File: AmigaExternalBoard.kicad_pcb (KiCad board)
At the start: 2 copper layers, 66.6 x 85.1 mm, 11 parts, among them J1 Conn_01x24, J2 Conn_01x24, J3 Conn_01x24

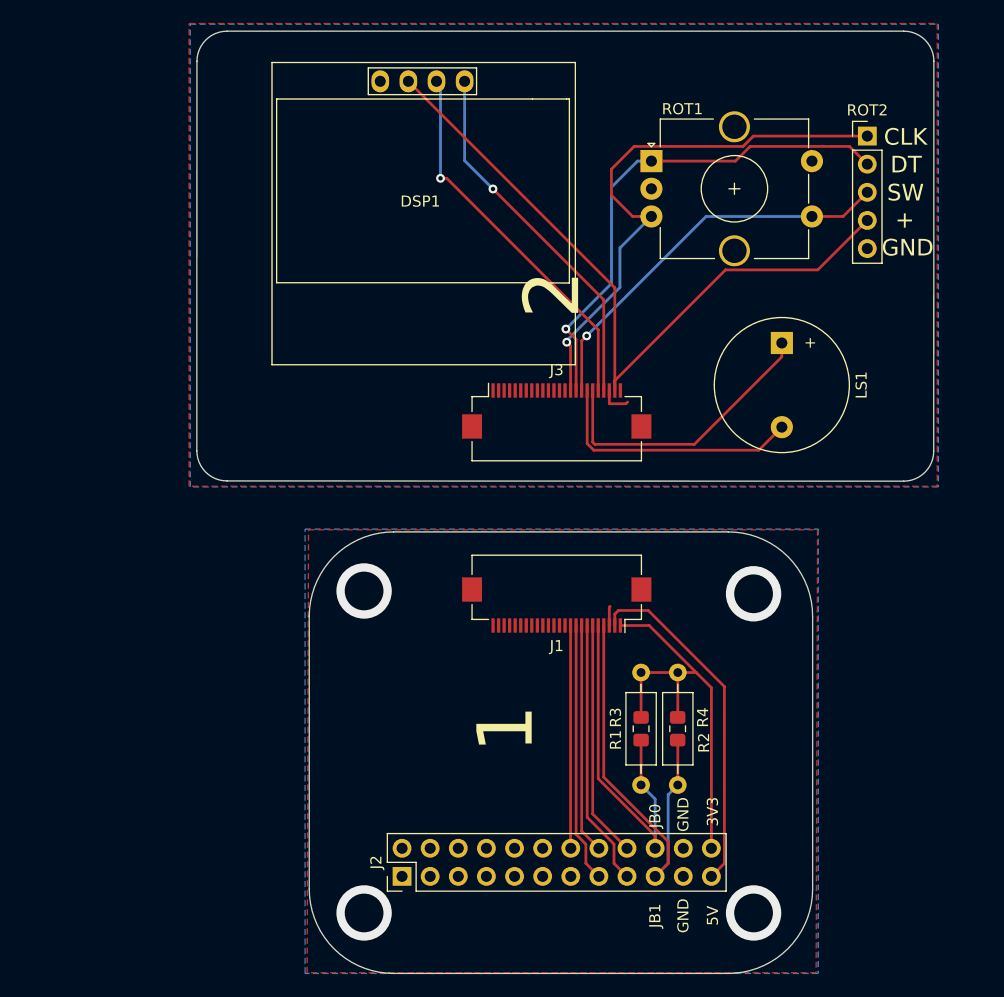
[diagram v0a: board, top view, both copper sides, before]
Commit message: Switches added
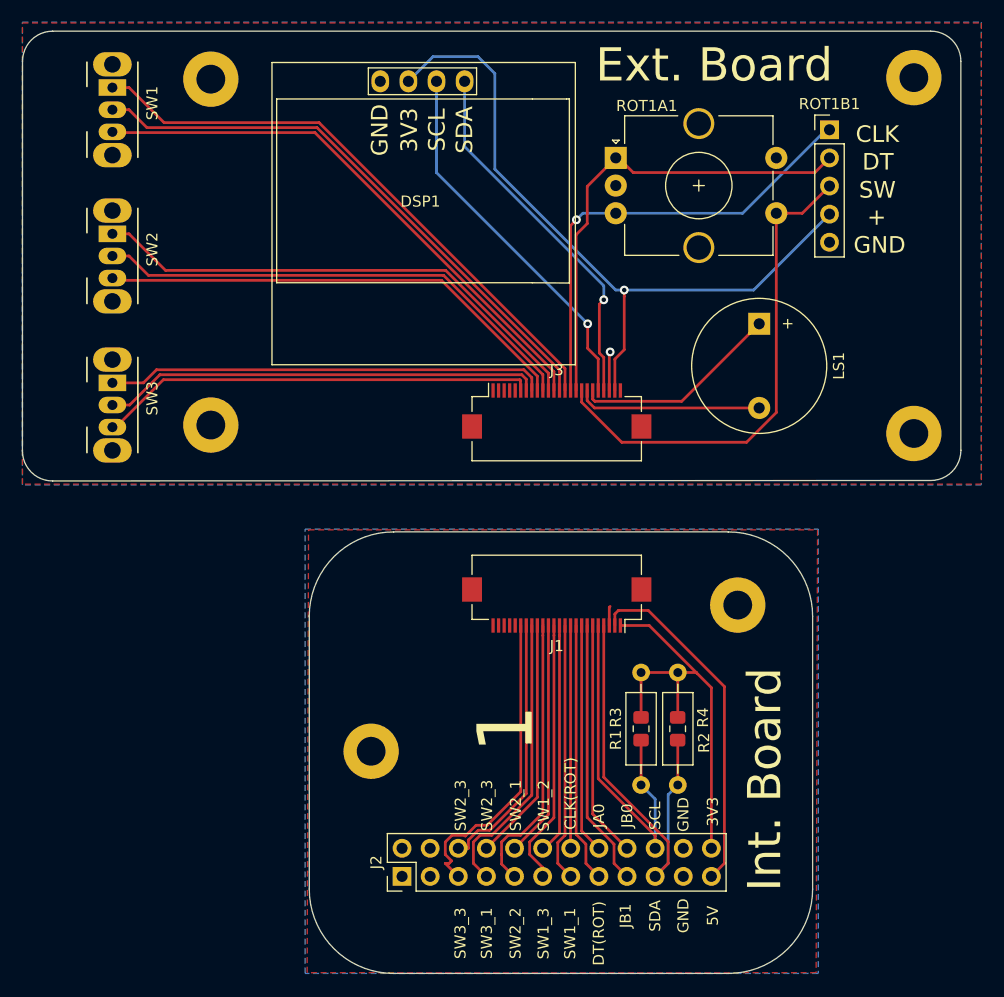
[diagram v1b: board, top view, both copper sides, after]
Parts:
- added REF**: MountingHole_3.5mm_Pad, MountingHole:MountingHole_3.5mm_Pad, F.Cu at (132.7, 107.7)
- added REF**: MountingHole_3.5mm_Pad, MountingHole:MountingHole_3.5mm_Pad, F.Cu at (99.6, 120.9)
- added REF**: MountingHole_3.5mm_Pad, MountingHole:MountingHole_3.5mm_Pad, F.Cu at (148.6, 92.2)
- added REF**: MountingHole_3.5mm_Pad, MountingHole:MountingHole_3.5mm_Pad, F.Cu at (85.1, 91.4)
- added REF**: MountingHole_3.5mm_Pad, MountingHole:MountingHole_3.5mm_Pad, F.Cu at (148.6, 60.1)
- added REF**: MountingHole_3.5mm_Pad, MountingHole:MountingHole_3.5mm_Pad, F.Cu at (85.1, 60.2)
- added SW1: SW_SPDT, Button_Switch_THT:SW_CuK_OS102011MA1QN1_SPDT_Angled, F.Cu at (76.2, 61.0)
- added SW2: SW_SPDT, Button_Switch_THT:SW_CuK_OS102011MA1QN1_SPDT_Angled, F.Cu at (76.2, 74.2)
- added SW3: SW_SPDT, Button_Switch_THT:SW_CuK_OS102011MA1QN1_SPDT_Angled, F.Cu at (76.2, 87.6)
- moved ROT1B1 3.46 mm to (141.0, 64.8)
- moved ROT1A1 3.23 mm to (121.7, 67.3)
- moved LS1 2.68 mm to (134.6, 82.3)
- renumbered ROT1 to ROT1A1, ROT2 to ROT1B1
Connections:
- J1 pad 11: Net-(J1-Pad11) -> SW1_1
- J1 pad 12: Net-(J1-Pad12) -> SW1_2
- J1 pad 13: Net-(J1-Pad13) -> SW1_3
- J1 pad 14: Net-(J1-Pad14) -> SW2_1
- J1 pad 15: Net-(J1-Pad15) -> SW2_2
- J1 pad 16: Net-(J1-Pad16) -> SW2_3
- J1 pad 17: Net-(J1-Pad17) -> SW3_1
- J1 pad 18: Net-(J1-Pad18) -> SW3_2
- J1 pad 19: Net-(J1-Pad19) -> SW3_3
- J2 pad 10: Net-(J2-Pad10) -> SW2_1
- J2 pad 11: Net-(J2-Pad11) -> SW1_3
- J2 pad 12: Net-(J2-Pad12) -> SW1_2
- J2 pad 13: Net-(J2-Pad13) -> SW1_1
- J2 pad 5: Net-(J2-Pad5) -> SW3_3
- J2 pad 6: Net-(J2-Pad6) -> SW3_2
- J2 pad 7: Net-(J2-Pad7) -> SW3_1
- J2 pad 8: Net-(J2-Pad8) -> SW2_3
- J2 pad 9: Net-(J2-Pad9) -> SW2_2
- J3 pad 10: Net-(J3-Pad10) -> SW2_2
- J3 pad 11: Net-(J3-Pad11) -> SW2_1
- J3 pad 12: Net-(J3-Pad12) -> SW1_3
- J3 pad 13: Net-(J3-Pad13) -> SW1_2
- J3 pad 14: Net-(J3-Pad14) -> SW1_1
- J3 pad 6: Net-(J3-Pad6) -> SW3_3
- J3 pad 7: Net-(J3-Pad7) -> SW3_2
- J3 pad 8: Net-(J3-Pad8) -> SW3_1
- J3 pad 9: Net-(J3-Pad9) -> SW2_3
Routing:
- net SW1_1: track 0.00 -> 76.8 mm
- net SW1_3: track 0.00 -> 74.6 mm
- net SW1_2: track 0.00 -> 72.8 mm
- net SW2_2: track 0.00 -> 70.1 mm
- net SW3_3: track 0.00 -> 67.6 mm
- net SW2_1: track 0.00 -> 67.6 mm
- net SW3_1: track 0.00 -> 65.8 mm
- net SW2_3: track 0.00 -> 65.4 mm
- net SW3_2: track 0.00 -> 63.5 mm
- net JA0(ROT-SW): track 56.6 -> 65.8 mm, vias 1 -> 0
- net CLK(ROT): track 70.3 -> 62.0 mm
- net JB0(SPK): track 47.8 -> 40.2 mm
- net JB1(SPK): track 47.6 -> 40.9 mm
- net DT(ROT): track 69.3 -> 66.4 mm, vias 1 -> 0
- net GND: track 4.67 -> 5.27 mm, vias 4 -> 1
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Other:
- board size 66.6 x 85.1 mm -> 84.8 x 85.1 mm
- board text added: "CLK(ROT)"
- board text added: "DT(ROT)"
- board text added: "Ext. Board"
- board text added: "Int. Board"
- board text added: "JA0"
- board text added: "SCL"
- board text added: "SDA"
- board text added: "SW1_1"
- board text added: "SW1_2"
- board text added: "SW1_3"
- board text added: "SW2_1"
- board text added: "SW2_2"
- board text added: "SW2_3"
- board text added: "SW3_1"
- board text added: "SW3_3"
- board text removed: "2"
